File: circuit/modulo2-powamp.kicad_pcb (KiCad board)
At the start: 2 copper layers, 105 x 47 mm, 74 parts, among them J1 HOLE, J2 HOLE, J3 HOLE, J4 HOLE, J5 CONN_01X04, SW1 reset, SW2 mute, SW3 HEAD/AD, U1 LM1117-5.0, U2 TPA3220, U3 MCP16331, U4 GAINSEL, U5 POWER

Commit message: getting closer to the final PCBs; still have to change the rotenc
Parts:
- removed SW2: mute, myAmp:Switch_2.5mm
- added Q1: BS170, myAmp:TO-92_Inline_Wide, F.Cu at (95.9, 87.6)
- added R17: 47K, myAmp:R_0805, F.Cu at (101.0, 85.7)
- added U6: AMPCTRL, myAmp:PIN_1x03, F.Cu at (95.0, 93.0)
- R10, R11, R12: footprint myAmp:R_0805 -> myAmp:R_10MM
- U5: value POWER -> PWR_CONN
- moved R12 17.1 mm to (81.9, 75.6), turned to 0 degrees
- moved R10 13.6 mm to (81.9, 78.1)
- moved R11 5.43 mm to (92.1, 64.8), turned to 90 degrees
- moved R13 3.24 mm to (92.7, 82.5)
- moved C15 2.84 mm to (87.0, 83.8)
- moved C14 2.84 mm to (81.3, 83.8)
- moved SW1 2.54 mm to (95.9, 69.8)
- moved J5 2.00 mm to (74.0, 93.0)
- moved C1 1.91 mm to (140.3, 59.7)
- moved C16 1.91 mm to (140.3, 78.7)
- moved C24 1.91 mm to (140.3, 88.9)
- moved C9 1.91 mm to (140.3, 69.2)
- moved C12 1.27 mm to (87.0, 69.8)
- moved C10 1.27 mm to (81.3, 69.8)
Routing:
- net /RESET: track 0.00 -> 57.1 mm
- net +5V: track 116.4 -> 159.3 mm, vias 0 -> 1
- net Net-(C10-Pad1): track 0.00 -> 27.6 mm
- net Net-(C10-Pad2): track 0.00 -> 26.9 mm
- net Net-(C12-Pad1): track 0.00 -> 26.7 mm
- net Net-(C14-Pad2): track 0.00 -> 26.4 mm
- net /FREQ_ADJ: track 0.00 -> 21.1 mm
- net Net-(C12-Pad2): track 0.00 -> 20.9 mm
- net Net-(C15-Pad2): track 0.00 -> 20.5 mm
- net /CMUTE: track 0.00 -> 19.5 mm
- net Net-(C15-Pad1): track 0.00 -> 12.0 mm
- net Net-(Q1-Pad2): track 0.00 -> 11.3 mm
- net HEAD: track 0.00 -> 9.92 mm
- net Net-(C14-Pad1): track 0.00 -> 9.17 mm
- net /GVDD: track 0.00 -> 6.50 mm
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
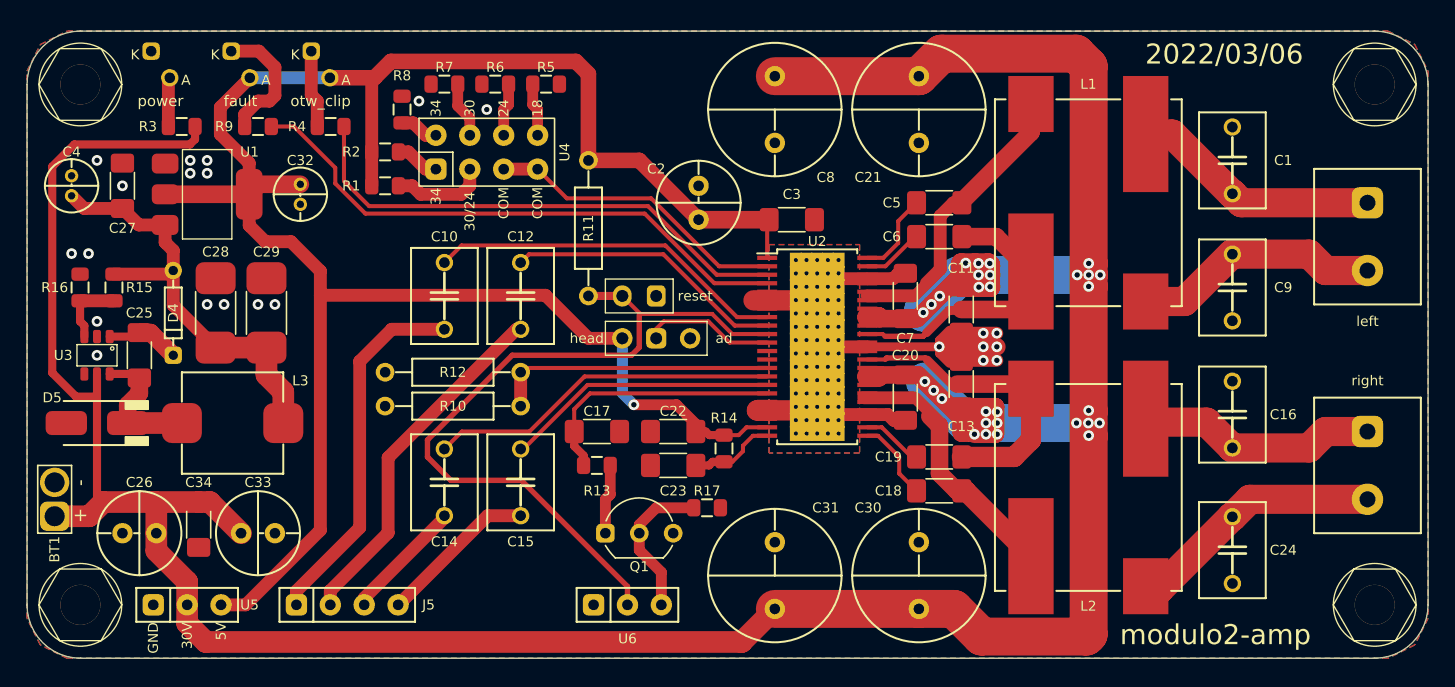
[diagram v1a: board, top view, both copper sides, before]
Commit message: found new switch for gain select; eq needs redesign
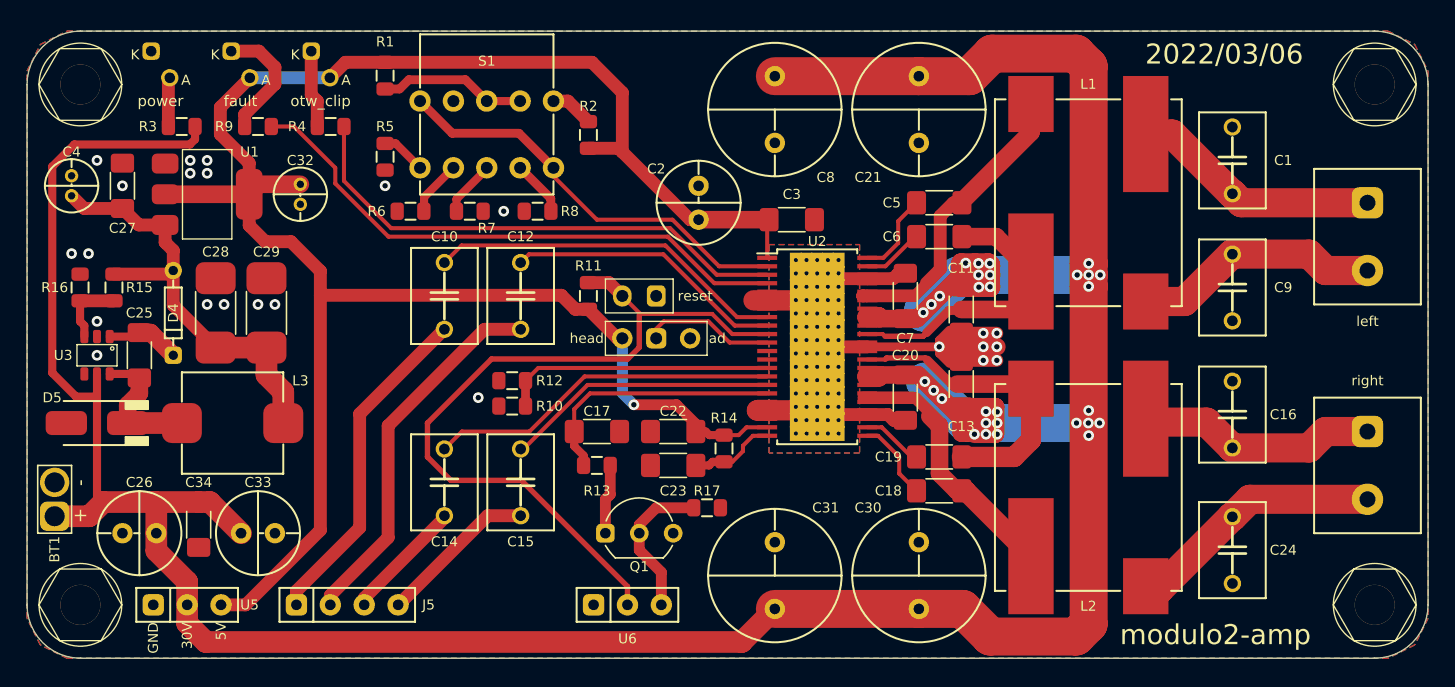
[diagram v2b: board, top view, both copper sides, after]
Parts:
- removed U4: GAINSEL, myAmp:GAINSEL
- added S1: GAINSEL, myAmp:SR10010F-0204, F.Cu at (84.5, 55.2)
- R10, R11, R12: footprint myAmp:R_10MM -> myAmp:R_0805
- moved R2 15.3 mm to (92.1, 57.8), turned to 90 degrees
- moved R5 13.2 mm to (76.8, 59.4), turned to -90 degrees
- moved R8 12.7 mm to (88.3, 63.5), turned to 180 degrees
- moved R6 11.4 mm to (78.7, 63.5)
- moved R7 9.71 mm to (83.2, 63.5), turned to 0 degrees
- moved R1 8.25 mm to (76.8, 53.3), turned to -90 degrees
- moved R11 5.08 mm to (92.1, 69.8), turned to -90 degrees
- moved R12 4.49 mm to (86.4, 76.2)
- moved R10 4.44 mm to (86.4, 78.1)
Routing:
- net Net-(U2-Pad2): track 22.8 -> 31.5 mm
- net +5V: track 159.3 -> 152.5 mm
- net Net-(R1-Pad2): track 7.13 -> 11.1 mm
- net Net-(C10-Pad1): track 27.6 -> 25.2 mm
- net /RESET: track 57.1 -> 58.6 mm
- net Net-(C12-Pad1): track 26.7 -> 28.1 mm
- net Net-(R8-Pad1): track 2.92 -> 4.21 mm
- net /FREQ_ADJ: track 21.1 -> 20.4 mm
- net /OUT1_P: track 22.5 -> 23.2 mm
- net Net-(R5-Pad1): track 3.98 -> 3.38 mm
- net Net-(D3-Pad1): track 9.67 -> 9.16 mm
- net GND: vias 23 -> 24

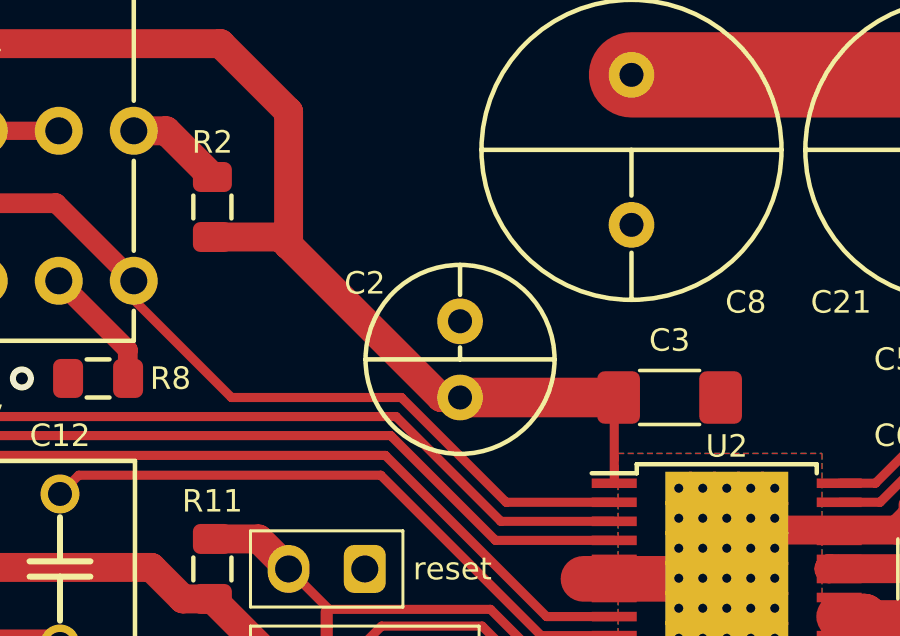
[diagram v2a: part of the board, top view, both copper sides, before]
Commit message: ditched the LED array board; LEDs are on the main PCB now
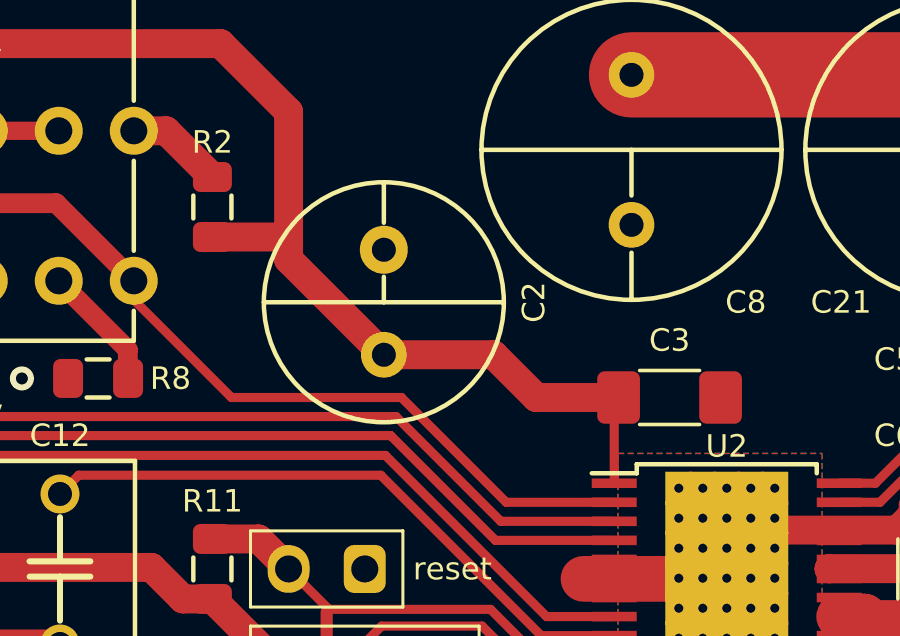
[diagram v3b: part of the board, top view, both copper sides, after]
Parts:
- C2: footprint myAmp:CPOL_D6.3_P2.5 -> myAmp:CPOL_D8_P3.5
- moved C2 3.17 mm to (97.8, 61.0)
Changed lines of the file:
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@@
   (net 29 "Net-(R8-Pad1)")
   (net 30 "Net-(Q1-Pad1)")
-  (net 31 "Net-(U2-Pad2)")
+  (net 31 "Net-(S1-Pad1)")
   (net 32 "HEAD")
   (net 33 "Net-(C10-Pad1)")
@@
   (net 53 "Net-(Q1-Pad2)")
   (net 54 "unconnected-(S1-Pad2)")
-  (footprint "myAmp:CPOL_D6.3_P2.5" (layer "F.Cu")
-    (at 100.33 62.865 90)
-    (property "Sheetfile" "modulo2-powamp.kicad_sch")
-    (property "Sheetname" "")
-    (attr through_hole)
-    (fp_text reference "C2" (at 2.54 -3.175 180) (layer "F.SilkS")
+  (footprint "myAmp:CPOL_D8_P3.5" (layer "F.Cu")
+    (at 97.79 60.96 90)
+    (property "Sheetfile" "modulo2-powamp.kicad_sch")
+    (property "Sheetname" "")
+    (attr through_hole)
+    (fp_text reference "C2" (at 0 5 90) (layer "F.SilkS")
       (effects (font (size 0.75 0.75) (thickness 0.15)))
     )
@@
       (effects (font (size 0.127 0.127) (thickness 0.03175)))
     )
-    (fp_line (start 3.15 0) (end 2.15 0) (layer "F.SilkS") (width 0.15))
-    (fp_line (start 0 -3.15) (end 0 3.15) (layer "F.SilkS") (width 0.15))
-    (fp_line (start 0 0) (end 0.4 0) (layer "F.SilkS") (width 0.15))
-    (fp_circle (center 0 0) (end 3.15 0) (layer "F.SilkS") (width 0.15) (fill none))
-    (pad "1" thru_hole circle locked (at -1.27 0 90) (size 1.524 1.524) (drill 0.8) (layers *.Cu *.Mask)
+    (fp_line (start 0 -4) (end 0 4) (layer "F.SilkS") (width 0.15))
+    (fp_line (start 4 0) (end 2.65 0) (layer "F.SilkS") (width 0.15))
+    (fp_line (start 0 0) (end 0.85 0) (layer "F.SilkS") (width 0.15))
+    (fp_circle (center 0 0) (end 4 0) (layer "F.SilkS") (width 0.15) (fill none))
+    (pad "1" thru_hole circle locked (at -1.75 0 90) (size 1.524 1.524) (drill 0.8) (layers *.Cu *.Mask)
       (net 3 "+5V") (pintype "passive"))
-    (pad "2" thru_hole circle locked (at 1.27 0 90) (size 1.524 1.524) (drill 0.8) (layers *.Cu *.Mask)
-      (net 1 "GND") (pintype "passive"))
-    (model "${KIPRJMOD}/myAmp.pretty/models/CP_Radial_D6.3mm_P2.50mm.step"
-      (offset (xyz -1.25 0 0))
+    (pad "2" thru_hole circle locked (at 1.75 0 90) (size 1.6 1.6) (drill 0.8) (layers *.Cu *.Mask)
+      (net 1 "GND") (pintype "passive"))
+    (model "${KIPRJMOD}/myAmp.pretty/models/CP_Radial_D8.0mm_P3.50mm.wrl"
+      (offset (xyz -1.75 0 0))
       (scale (xyz 1 1 1))
       (rotate (xyz 0 0 0))
@@
       (net 3 "+5V") (pinfunction "VDD") (pintype "bidirectional"))
     (pad "2" smd rect locked (at -3.75 -6.0325) (size 1.5 0.32) (layers "F.Cu" "F.Paste" "F.Mask")
-      (net 31 "Net-(U2-Pad2)") (pinfunction "GAIN/SLV") (pintype "input"))
+      (net 31 "Net-(S1-Pad1)") (pinfunction "GAIN/SLV") (pintype "input"))
     (pad "3" smd rect locked (at -3.75 -5.3975) (size 1.5 0.32) (layers "F.Cu" "F.Paste" "F.Mask")
       (net 21 "OTW_CLIP") (pinfunction "~{OTW_CLIP}") (pintype "output"))
@@
     (fp_line (start 5 1) (end 5 4) (layer "F.SilkS") (width 0.15))
     (pad "1" thru_hole circle (at -5 0) (size 1.6 1.6) (drill 0.9) (layers *.Cu *.Mask)
-      (net 31 "Net-(U2-Pad2)") (pintype "passive"))
+      (net 31 "Net-(S1-Pad1)") (pintype "passive"))
     (pad "2" thru_hole circle (at -2.5 0) (size 1.6 1.6) (drill 0.9) (layers *.Cu *.Mask)
       (net 54 "unconnected-(S1-Pad2)") (pintype "passive+no_connect"))
@@
       (net 29 "Net-(R8-Pad1)") (pintype "passive"))
     (pad "10" thru_hole circle (at 5 5) (size 1.6 1.6) (drill 0.9) (layers *.Cu *.Mask)
-      (net 31 "Net-(U2-Pad2)") (pintype "passive"))
+      (net 31 "Net-(S1-Pad1)") (pintype "passive"))
   )
   (footprint "myAmp:PIN_1x03" (layer "F.Cu")
@@
   (segment (start 98.679 78.0034) (end 95.4786 78.0034) (width 0.8128) (layer "F.Cu") (net 3))
   (segment (start 67.8688 65.786) (end 66.65 64.5672) (width 0.9652) (layer "F.Cu") (net 3))
-  (segment (start 94.615 59.055) (end 94.615 54.61) (width 0.9652) (layer "F.Cu") (net 3))
   (segment (start 105.47 79.6925) (end 103.9241 79.6925) (width 0.3048) (layer "F.Cu") (net 3))
   (segment (start 66.65 64.5672) (end 66.65 62.23) (width 0.9652) (layer "F.Cu") (net 3))
   (segment (start 71.9836 69.7992) (end 71.9836 67.9836) (width 0.9652) (layer "F.Cu") (net 3))
-  (segment (start 99.695 64.135) (end 94.615 59.055) (width 0.9652) (layer "F.Cu") (net 3))
   (segment (start 66.7 53.5) (end 64.4906 55.7094) (width 0.9652) (layer "F.Cu") (net 3))
   (segment (start 105.47 66.9925) (end 105.47 64.28) (width 0.3048) (layer "F.Cu") (net 3))
+  (segment (start 92.345 52.34) (end 76.835 52.34) (width 0.9652) (layer "F.Cu") (net 3))
   (segment (start 94.25 73.025) (end 92.075 70.85) (width 0.9652) (layer "F.Cu") (net 3))
+  (segment (start 102.87 64.135) (end 105.615 64.135) (width 0.9652) (layer "F.Cu") (net 3))
   (segment (start 73.86 52.34) (end 72.7 53.5) (width 0.9652) (layer "F.Cu") (net 3))
-  (segment (start 94.615 54.61) (end 92.345 52.34) (width 0.9652) (layer "F.Cu") (net 3))
   (segment (start 76.835 52.34) (end 73.86 52.34) (width 0.9652) (layer "F.Cu") (net 3))
+  (segment (start 101.445 62.71) (end 102.87 64.135) (width 0.9652) (layer "F.Cu") (net 3))
   (segment (start 71.9836 69.7992) (end 90.043 69.7992) (width 0.9652) (layer "F.Cu") (net 3))
   (segment (start 103.3366 80.28) (end 102.235 80.28) (width 0.3048) (layer "F.Cu") (net 3))
   (segment (start 64.4906 55.7094) (end 64.4906 57.7342) (width 0.9652) (layer "F.Cu") (net 3))
-  (segment (start 94.345 58.785) (end 94.615 59.055) (width 0.9652) (layer "F.Cu") (net 3))
+  (segment (start 92.075 58.785) (end 94.345 58.785) (width 0.9652) (layer "F.Cu") (net 3))
+  (segment (start 94.615 59.535) (end 94.615 59.055) (width 0.9652) (layer "F.Cu") (net 3))
+  (segment (start 97.79 62.71) (end 94.615 59.535) (width 0.9652) (layer "F.Cu") (net 3))
   (segment (start 69.786 65.786) (end 67.8688 65.786) (width 0.9652) (layer "F.Cu") (net 3))
   (segment (start 71.9836 87.4014) (end 71.9836 69.7992) (width 0.9652) (layer "F.Cu") (net 3))
   (segment (start 100.125 79.4494) (end 98.679 78.0034) (width 0.8128) (layer "F.Cu") (net 3))
   (segment (start 64.4906 57.7342) (end 66.65 59.8936) (width 0.9652) (layer "F.Cu") (net 3))
+  (segment (start 94.345 58.785) (end 94.615 59.055) (width 0.9652) (layer "F.Cu") (net 3))
   (segment (start 71.9836 67.9836) (end 69.786 65.786) (width 0.9652) (layer "F.Cu") (net 3))
-  (segment (start 92.345 52.34) (end 76.835 52.34) (width 0.9652) (layer "F.Cu") (net 3))
   (segment (start 70.485 61.48) (end 67.4 61.48) (width 1.3208) (layer "F.Cu") (net 3))
   (segment (start 101.1334 80.28) (end 102.235 80.28) (width 0.6096) (layer "F.Cu") (net 3))
@@
   (segment (start 66.65 59.8936) (end 66.65 62.23) (width 0.9652) (layer "F.Cu") (net 3))
   (segment (start 100.8634 80.01) (end 101.1334 80.28) (width 0.6096) (layer "F.Cu") (net 3))
+  (segment (start 97.79 62.71) (end 101.445 62.71) (width 0.9652) (layer "F.Cu") (net 3))
   (segment (start 60.35 62.23) (end 66.65 62.23) (width 1.3208) (layer "F.Cu") (net 3))
-  (segment (start 100.33 64.135) (end 99.695 64.135) (width 0.9652) (layer "F.Cu") (net 3))
-  (segment (start 92.075 58.785) (end 94.345 58.785) (width 0.9652) (layer "F.Cu") (net 3))
   (segment (start 100.125 80.01) (end 100.125 79.4494) (width 0.8128) (layer "F.Cu") (net 3))
   (segment (start 100.125 80.01) (end 100.8634 80.01) (width 0.6096) (layer "F.Cu") (net 3))
   (segment (start 94.615 73.025) (end 94.25 73.025) (width 0.9652) (layer "F.Cu") (net 3))
-  (segment (start 100.33 64.135) (end 105.615 64.135) (width 1.3208) (layer "F.Cu") (net 3))
+  (segment (start 94.615 59.055) (end 94.615 54.61) (width 0.9652) (layer "F.Cu") (net 3))
   (segment (start 64.54 93) (end 66.385 93) (width 0.9652) (layer "F.Cu") (net 3))
+  (segment (start 94.615 54.61) (end 92.345 52.34) (width 0.9652) (layer "F.Cu") (net 3))
   (segment (start 105.47 64.28) (end 105.615 64.135) (width 0.3048) (layer "F.Cu") (net 3))
   (segment (start 103.9241 79.6925) (end 103.3366 80.28) (width 0.3048) (layer "F.Cu") (net 3))

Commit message: almost there...
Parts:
- moved D2 7.00 mm to (79.0, 50.5)
- moved R2 6.54 mm to (97.8, 54.6), turned to -90 degrees
- moved R4 5.98 mm to (78.7, 57.1)
- moved R1 5.72 mm to (82.5, 53.3)
- moved R5 5.72 mm to (82.5, 59.4)
- moved S1 5.72 mm to (90.2, 55.2)
- moved R6 5.08 mm to (83.8, 63.5)
- moved R7 5.08 mm to (88.3, 63.5)
- moved R8 5.08 mm to (93.3, 63.5)
- moved C2 3.70 mm to (100.5, 63.5), turned to 180 degrees
- moved D3 3.50 mm to (69.5, 50.5)
- moved R9 1.91 mm to (69.2, 57.1)
- moved C21 0.64 mm to (116.8, 55.2)
- moved C8 0.64 mm to (106.0, 55.2)
- moved C30 0.63 mm to (116.8, 91.4)
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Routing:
- net OTW_CLIP: track 38.7 -> 33.5 mm
- net +5V: track 152.8 -> 147.8 mm
- net Net-(S1-Pad1): track 31.5 -> 27.3 mm
- net +BATT: track 277.5 -> 274.6 mm
- net FAULT: track 42.7 -> 40.1 mm
- net /OUT1_M: track 18.4 -> 19.9 mm
- net Net-(D3-Pad1): track 9.16 -> 9.69 mm
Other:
- board text added: "GND"
- board text added: "IL+"
- board text added: "IL-"
- board text added: "IR+"
- board text added: "IR-"
- board text added: "MUT"
- board text added: "RST"

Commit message: sent to fab!
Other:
- board text added: "2022/2/27"
- board text removed: "2022/03/06"
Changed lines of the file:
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@@
       (usegerberattributes true)
       (usegerberadvancedattributes true)
-      (creategerberjobfile false)
+      (creategerberjobfile true)
       (svguseinch false)
       (svgprecision 6)
@@
     (effects (font (size 0.75 0.75) (thickness 0.15)) (justify right))
   )
-  (gr_text "2022/03/06" (at 132.715 51.7398) (layer "F.SilkS")
+  (gr_text "2022/2/27" (at 137.16 51.7398) (layer "F.SilkS")
     (effects (font (size 2 2) (thickness 0.3)))
   )
